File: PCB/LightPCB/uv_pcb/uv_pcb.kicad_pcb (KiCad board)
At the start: 2 copper layers, 28 x 51.9 mm, 32 parts, among them J1 Conn_01x12, J2 Conn_01x08, Q1 2N7002, Q2 2N7002, U1 AP2112K-3.3V

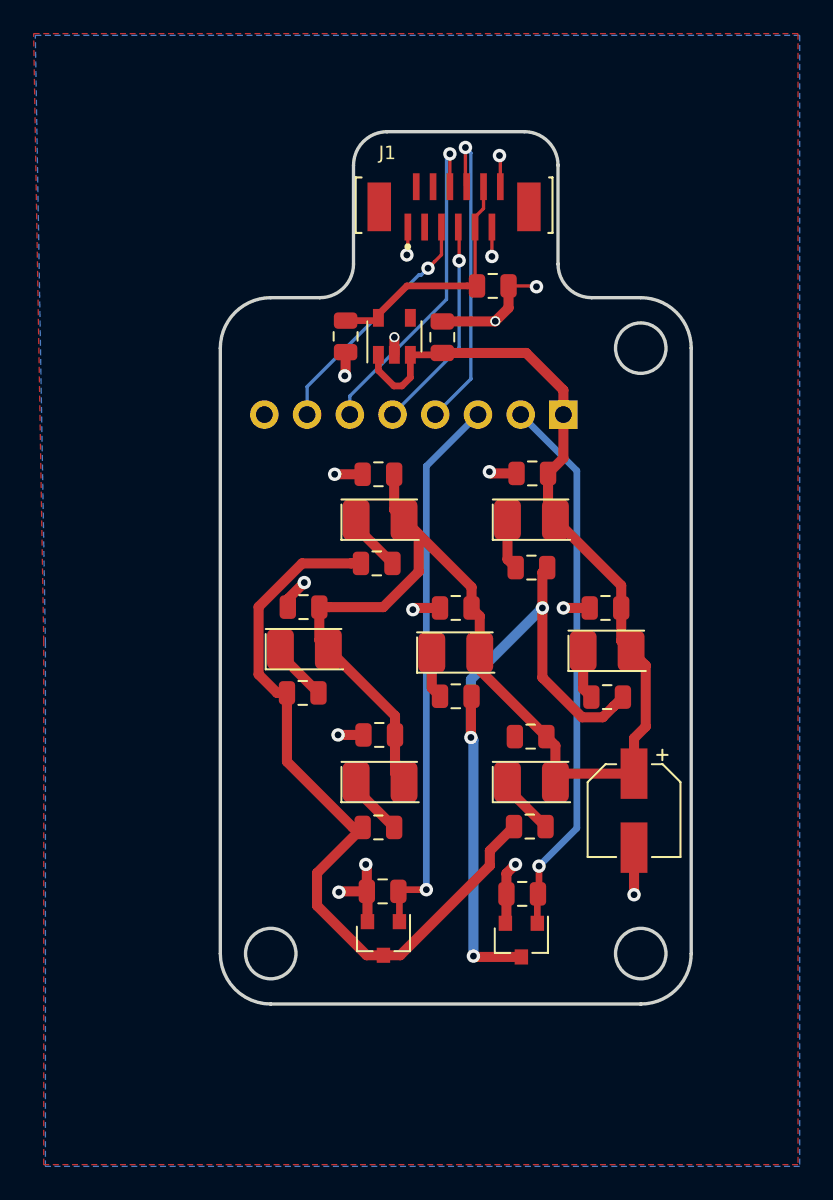
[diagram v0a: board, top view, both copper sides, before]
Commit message: added reset to PCB
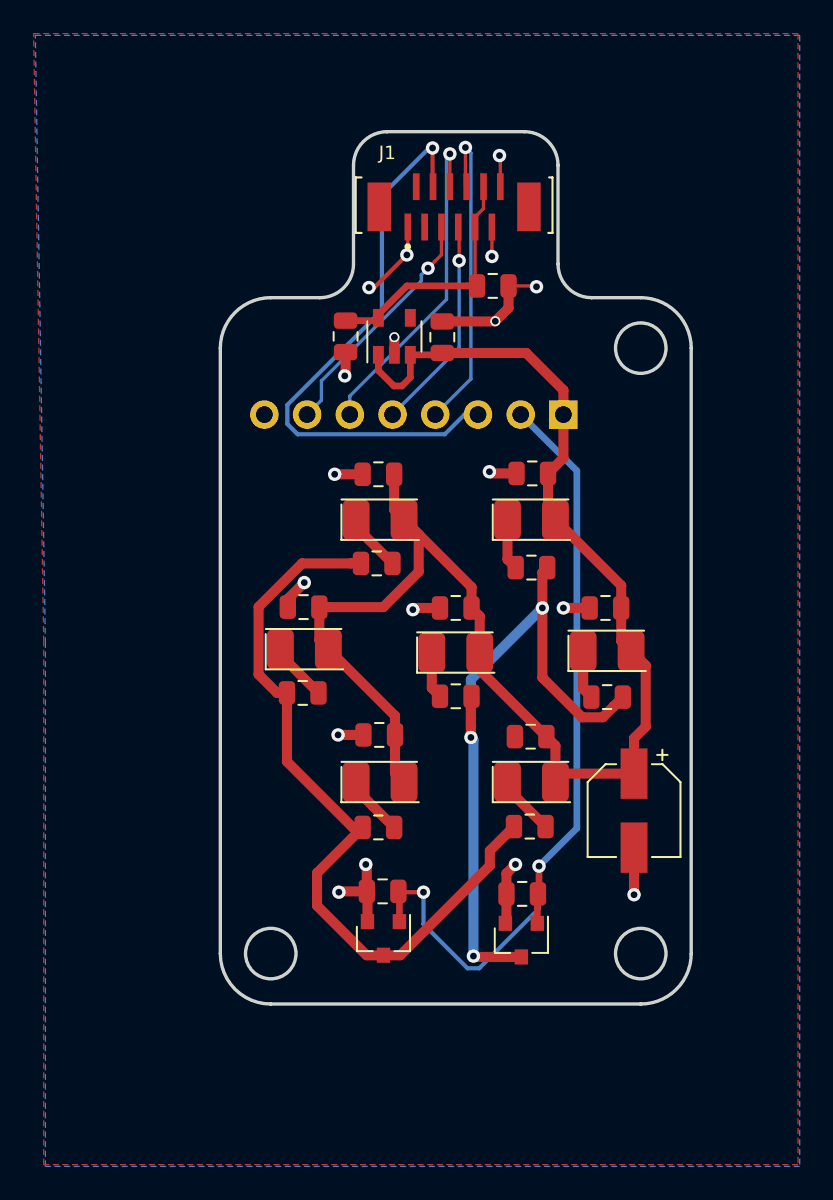
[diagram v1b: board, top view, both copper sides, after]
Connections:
- J1 pad 4: Net-(J1-Pad4) -> RST
- J2 pad 3: SW2 -> RST
- Q2 pad 1: SW2 -> SW1
- R9 pad 2: SW2 -> SW1
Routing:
- net RST: track 0.00 -> 34.5 mm, vias 0 -> 1
- net SW2: track 33.1 -> 0.00 mm, vias 1 -> 0
- net SW1: track 32.6 -> 49.8 mm, vias 1 -> 2
- net GND: track 36.6 -> 39.7 mm, vias 17 -> 18
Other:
- board text added: "RST"
- board text added: "UV"
- board text removed: "SW1"
- board text removed: "SW2"
